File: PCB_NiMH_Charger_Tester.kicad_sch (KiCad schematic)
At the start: 63 parts, among them J1 USB_C_Receptacle_PowerOnly_6P, J2 USB_C_Receptacle_USB2.0_16P, J3 UPDI v2 header, J4 SSD1306, J5 Serial Header, Q1 DTC114EL, Q2 DTA114EL, Q3 MTB060P06I3, Q4 MTA100N10KRI3, SW1 SW_Push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

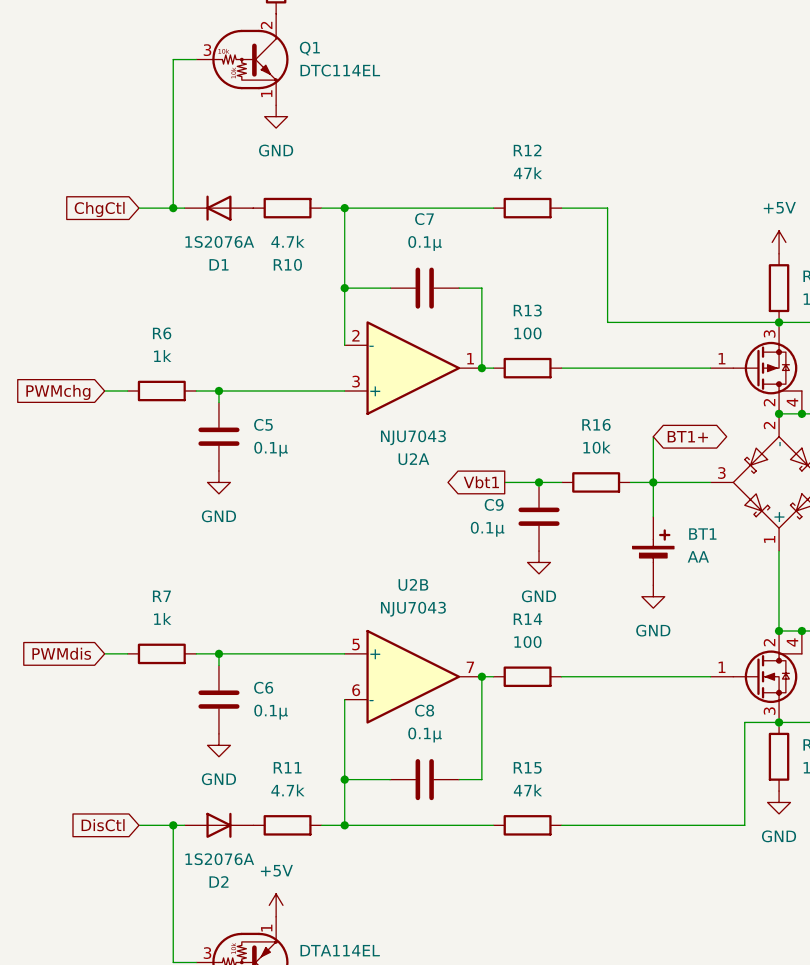
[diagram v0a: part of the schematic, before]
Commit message: Revert resistor values
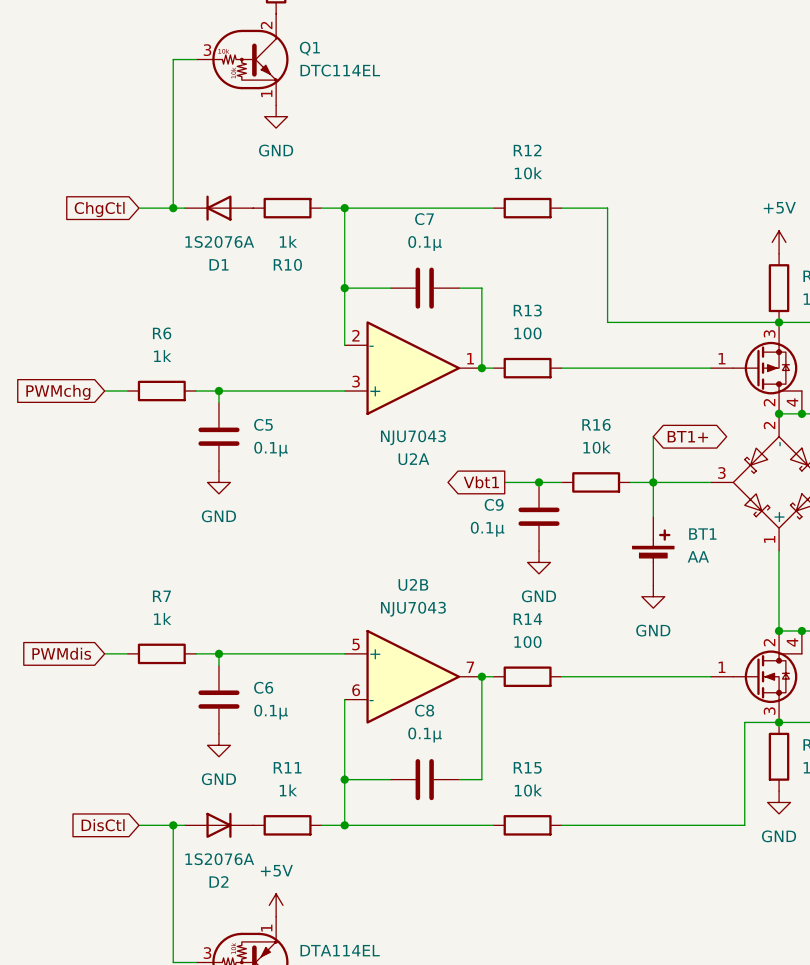
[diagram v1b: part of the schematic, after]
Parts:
- R10, R11: value 4.7k -> 1k
- R12, R15: value 47k -> 10k
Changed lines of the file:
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@@
 	(title_block
 		(title "NiMH Charger & Tester")
-		(date "2025-09-26")
+		(date "2025-10-15")
 		(rev "2")
 		(company "K.Takata")
@@
 			)
 		)
-		(property "Value" "47k"
+		(property "Value" "10k"
 			(at 156.21 152.4 90)
 			(effects
@@
 			)
 		)
-		(property "Value" "4.7k"
+		(property "Value" "1k"
 			(at 129.54 91.44 90)
 			(effects
@@
 			)
 		)
-		(property "Value" "47k"
+		(property "Value" "10k"
 			(at 156.21 83.82 90)
 			(effects
@@
 			)
 		)
-		(property "Value" "4.7k"
+		(property "Value" "1k"
 			(at 129.54 152.4 90)
 			(effects

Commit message: Fix D6 footprint
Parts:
- D6: footprint Package_DIP:DIP-4_W7.62mm -> Diode_THT:Diode_Bridge_DIP-4_W5.08mm_P2.54mm
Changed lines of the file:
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@@
 			)
 		)
-		(property "Footprint" "Package_DIP:DIP-4_W7.62mm"
+		(property "Footprint" "Diode_THT:Diode_Bridge_DIP-4_W5.08mm_P2.54mm"
 			(at 248.285 121.92 0)
 			(effects
